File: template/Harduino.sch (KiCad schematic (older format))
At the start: 24 parts, among them J1 2, J10 11, J11 12, J12 13, J13 A0, J14 A1, J15 A2, J16 A3, J17 A4, J18 A5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

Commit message: Add description Fix template
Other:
- moved on the sheet: H1, H2, H3, H4, J1, J10, J11, J12, J13, J14, J15, J16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

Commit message: Fix template
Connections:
- net VCC: now reaches J19.1 (Pin_1)
- net GND: now reaches J20.1 (Pin_1)
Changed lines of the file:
@@
 	1    0    0    -1
 $EndComp
+$Comp
+L power:GND #PWR0101
+U 1 1 5E4E1E07
+P 6550 3750
+F 0 "#PWR0101" H 6550 3500 50  0001 C CNN
+F 1 "GND" H 6555 3577 50  0000 C CNN
+F 2 "" H 6550 3750 50  0001 C CNN
+F 3 "" H 6550 3750 50  0001 C CNN
+	1    6550 3750
+	1    0    0    -1
+$EndComp
+$Comp
+L power:VCC #PWR0102
+U 1 1 5E4E268A
+P 6550 3500
+F 0 "#PWR0102" H 6550 3350 50  0001 C CNN
+F 1 "VCC" H 6567 3673 50  0000 C CNN
+F 2 "" H 6550 3500 50  0001 C CNN
+F 3 "" H 6550 3500 50  0001 C CNN
+	1    6550 3500
+	1    0    0    -1
+$EndComp
+Wire Wire Line
+	6550 3500 6550 3550
+Wire Wire Line
+	6550 3550 6750 3550
+Wire Wire Line
+	6750 3700 6550 3700
+Wire Wire Line
+	6550 3700 6550 3750
+$Comp
+L power:PWR_FLAG #FLG0101
+U 1 1 5E4E36FF
+P 6550 3550
+F 0 "#FLG0101" H 6550 3625 50  0001 C CNN
+F 1 "PWR_FLAG" V 6550 3677 50  0000 L CNN
+F 2 "" H 6550 3550 50  0001 C CNN
+F 3 "~" H 6550 3550 50  0001 C CNN
+	1    6550 3550
+	0    -1   -1   0
+$EndComp
+$Comp
+L power:PWR_FLAG #FLG0102
+U 1 1 5E4E3D09
+P 6550 3700
+F 0 "#FLG0102" H 6550 3775 50  0001 C CNN
+F 1 "PWR_FLAG" V 6550 3827 50  0000 L CNN
+F 2 "" H 6550 3700 50  0001 C CNN
+F 3 "~" H 6550 3700 50  0001 C CNN
+	1    6550 3700
+	0    -1   -1   0
+$EndComp
+Connection ~ 6550 3550
+Connection ~ 6550 3700
 $EndSCHEMATC

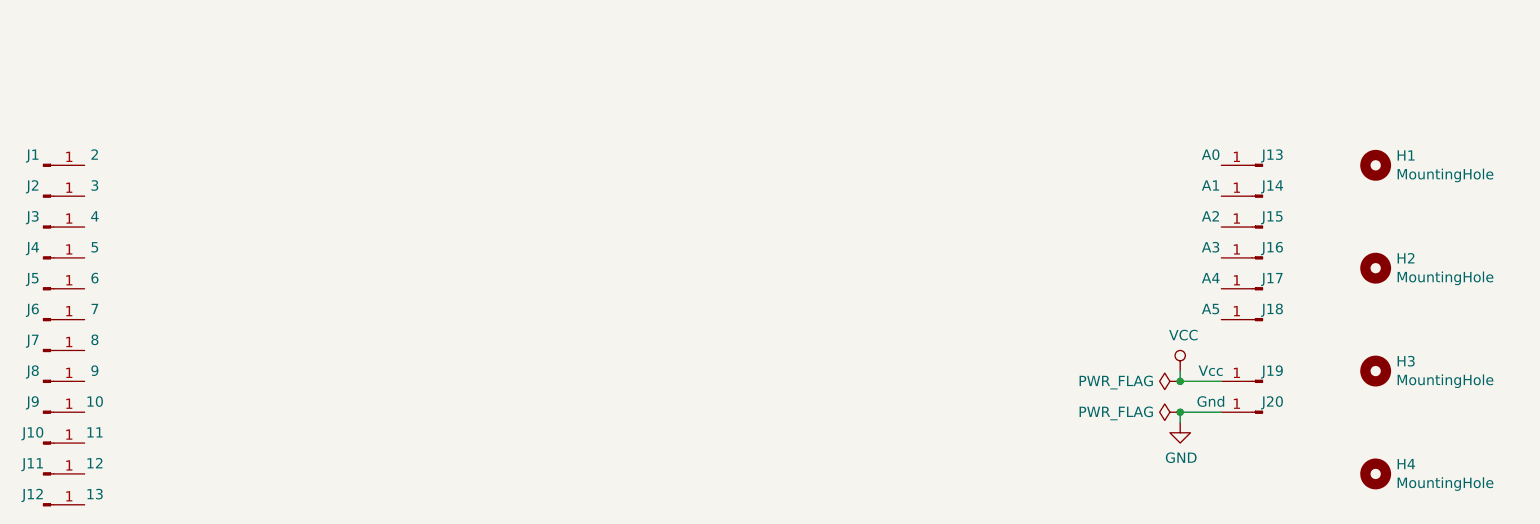
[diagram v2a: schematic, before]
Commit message: Replace 10 x 1pin sockets -> 1 x 10pin socket
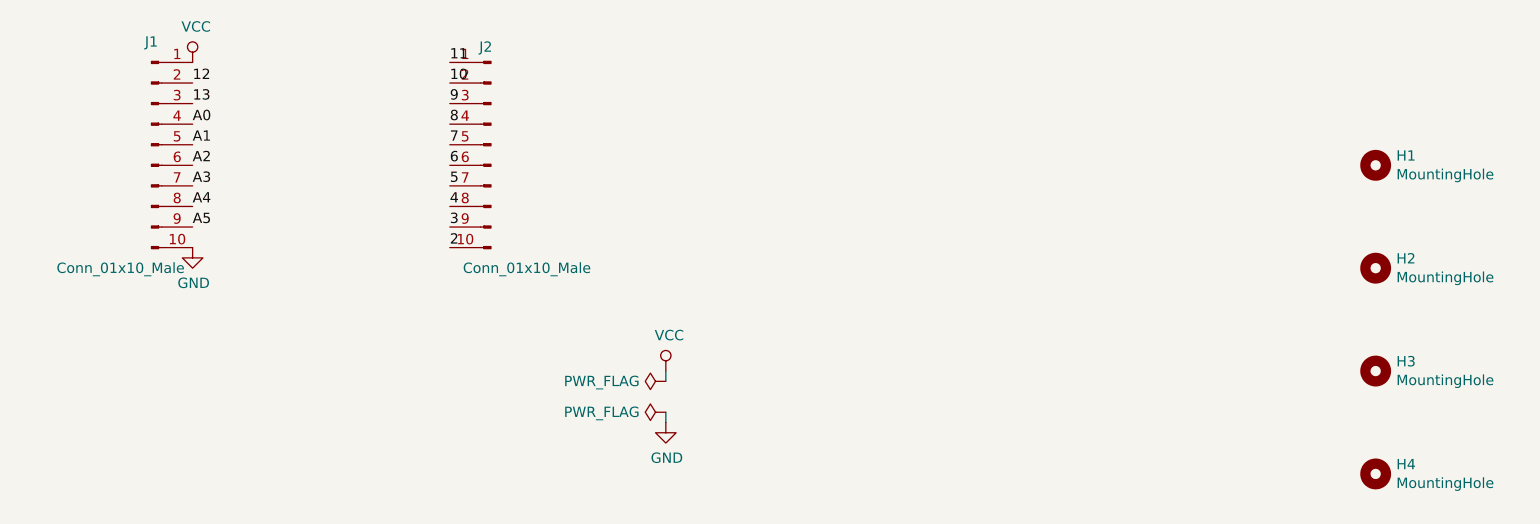
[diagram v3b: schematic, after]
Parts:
- removed J1: 2, Connector_PinHeader_2.54mm:PinHeader_1x01_P2.54mm_Vertical, symbol Connector:Conn_01x01_Male
- removed J10: 11, Connector_PinHeader_2.54mm:PinHeader_1x01_P2.54mm_Vertical, symbol Connector:Conn_01x01_Male
- removed J11: 12, Connector_PinHeader_2.54mm:PinHeader_1x01_P2.54mm_Vertical, symbol Connector:Conn_01x01_Male
- removed J12: 13, Connector_PinHeader_2.54mm:PinHeader_1x01_P2.54mm_Vertical, symbol Connector:Conn_01x01_Male
- removed J13: A0, Connector_PinHeader_2.54mm:PinHeader_1x01_P2.54mm_Vertical, symbol Connector:Conn_01x01_Male
- removed J14: A1, Connector_PinHeader_2.54mm:PinHeader_1x01_P2.54mm_Vertical, symbol Connector:Conn_01x01_Male
- removed J15: A2, Connector_PinHeader_2.54mm:PinHeader_1x01_P2.54mm_Vertical, symbol Connector:Conn_01x01_Male
- removed J16: A3, Connector_PinHeader_2.54mm:PinHeader_1x01_P2.54mm_Vertical, symbol Connector:Conn_01x01_Male
- removed J17: A4, Connector_PinHeader_2.54mm:PinHeader_1x01_P2.54mm_Vertical, symbol Connector:Conn_01x01_Male
- removed J18: A5, Connector_PinHeader_2.54mm:PinHeader_1x01_P2.54mm_Vertical, symbol Connector:Conn_01x01_Male
- removed J19: Vcc, Connector_PinHeader_2.54mm:PinHeader_1x01_P2.54mm_Vertical, symbol Connector:Conn_01x01_Male
- removed J2: 3, Connector_PinHeader_2.54mm:PinHeader_1x01_P2.54mm_Vertical, symbol Connector:Conn_01x01_Male
- removed J20: Gnd, Connector_PinHeader_2.54mm:PinHeader_1x01_P2.54mm_Vertical, symbol Connector:Conn_01x01_Male
- removed J3: 4, Connector_PinHeader_2.54mm:PinHeader_1x01_P2.54mm_Vertical, symbol Connector:Conn_01x01_Male
- removed J4: 5, Connector_PinHeader_2.54mm:PinHeader_1x01_P2.54mm_Vertical, symbol Connector:Conn_01x01_Male
- removed J5: 6, Connector_PinHeader_2.54mm:PinHeader_1x01_P2.54mm_Vertical, symbol Connector:Conn_01x01_Male
- removed J6: 7, Connector_PinHeader_2.54mm:PinHeader_1x01_P2.54mm_Vertical, symbol Connector:Conn_01x01_Male
- removed J7: 8, Connector_PinHeader_2.54mm:PinHeader_1x01_P2.54mm_Vertical, symbol Connector:Conn_01x01_Male
- removed J8: 9, Connector_PinHeader_2.54mm:PinHeader_1x01_P2.54mm_Vertical, symbol Connector:Conn_01x01_Male
- removed J9: 10, Connector_PinHeader_2.54mm:PinHeader_1x01_P2.54mm_Vertical, symbol Connector:Conn_01x01_Male
- added J1, J2: Conn_01x10_Male, Connector_PinSocket_2.54mm:PinSocket_1x10_P2.54mm_Vertical, symbol Connector:Conn_01x10_Male
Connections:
- net GND: now also J1.10 (Pin_10)
- net VCC: now also J1.1 (Pin_1)
- new net 10: J2.2 (Pin_2)
- new net 11: J2.1 (Pin_1)
- new net 12: J1.2 (Pin_2)
- new net 13: J1.3 (Pin_3)
- new net 2: J2.10 (Pin_10)
- new net 3: J2.9 (Pin_9)
- new net 4: J2.8 (Pin_8)
- new net 5: J2.7 (Pin_7)
- new net 6: J2.6 (Pin_6)
- new net 7: J2.5 (Pin_5)
- new net 8: J2.4 (Pin_4)
- new net 9: J2.3 (Pin_3)
- new net A0: J1.4 (Pin_4)
- new net A1: J1.5 (Pin_5)
- new net A2: J1.6 (Pin_6)
- new net A3: J1.7 (Pin_7)
- new net A4: J1.8 (Pin_8)
- new net A5: J1.9 (Pin_9)
